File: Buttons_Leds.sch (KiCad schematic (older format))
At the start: 38 parts, among them P11 CONN_01X06, P12 CONN_01X06, Q2 2N7002, Q3 2N7002, Q4 2N7002, Q5 2N7002, SW1 TEC_1, SW2 TEC_1, SW3 TEC_1, SW4 TEC_1

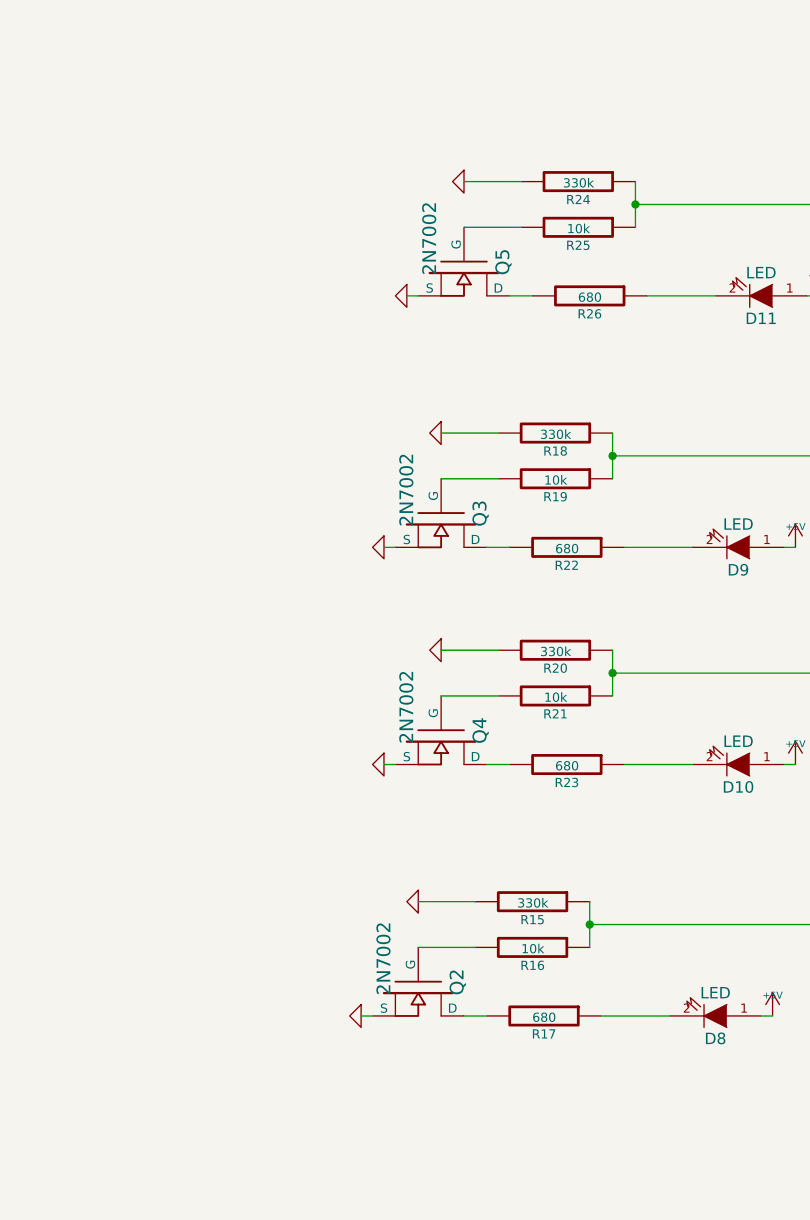
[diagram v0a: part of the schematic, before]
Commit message: Modifico algunos componentes. Seteo algunos encapsulados. Ordeno los componentes en el PCB.
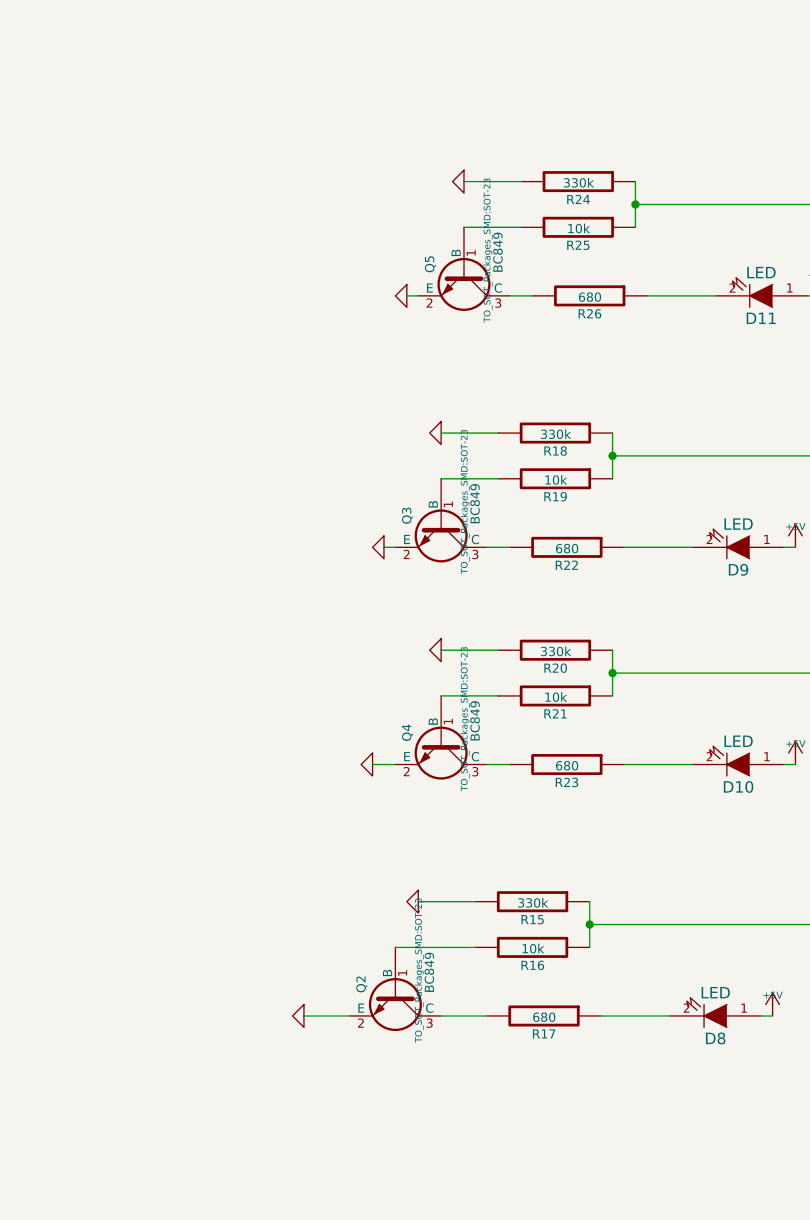
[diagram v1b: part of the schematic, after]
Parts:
- removed Q2, Q3, Q4, Q5: 2N7002, SOT23GDS, symbol MOSFET_N
- added Q2, Q3, Q4, Q5: BC849, TO_SOT_Packages_SMD:SOT-23, symbol BC849
- C10, C11, C12, C9: footprint c_0805 -> Capacitors_SMD:C_0805
- D10, D11, D8, D9: footprint LED-0805 -> LEDs:LED_1206
- P11, P12: footprint (none) -> Pin_Headers:Pin_Header_Angled_1x06
- R10, R11, R12, R13, R14, R15, R16, R17, R18, R19, R20, R21, R22, R23, R24, R25, R26, R7, R8, R9: footprint SM0805 -> SMD_Packages:SMD-1206_Pol
- SW1, SW2, SW3, SW4: footprint PUSH_SWITCH_THT -> Buttons_Switches_SMD:SW_SPST_KMR2
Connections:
- net GND: now also Q2.2 (E), Q3.2 (E), Q4.2 (E), Q5.2 (E)
- net at R23.2: now also Q4.3 (C)
- net at R21.2: now also Q4.1 (B)
- net at R17.2: now also Q2.3 (C)
- net at R16.2: now also Q2.1 (B)
- net at R26.2: now also Q5.3 (C)
- net at R25.2: now also Q5.1 (B)
- net at R22.2: now also Q3.3 (C)
- net at R19.2: now also Q3.1 (B)

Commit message: Algunas modificaciones en el circuito  oreno el pcb.
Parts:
- P11, P12: footprint Pin_Headers:Pin_Header_Angled_1x06 -> Pin_Headers:Pin_Header_Straight_1x06
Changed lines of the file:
@@
 LIBS:video
 LIBS:xilinx
+LIBS:sim800l
 EELAYER 25 0
 EELAYER END
@@
 $EndComp
 $Comp
-L GND #PWR042
+L GND #PWR037
 U 1 1 581A1B02
 P 6050 4250
-F 0 "#PWR042" H 6050 4250 30  0001 C CNN
+F 0 "#PWR037" H 6050 4250 30  0001 C CNN
 F 1 "GND" H 6050 4180 30  0001 C CNN
 F 2 "" H 6050 4250 60  0000 C CNN
@@
 $EndComp
 $Comp
-L +5V #PWR043
+L +5V #PWR038
 U 1 1 581A1B04
 P 7900 4250
-F 0 "#PWR043" H 7900 4340 20  0001 C CNN
+F 0 "#PWR038" H 7900 4340 20  0001 C CNN
 F 1 "+5V" H 7900 4340 30  0000 C CNN
 F 2 "" H 7900 4250 60  0000 C CNN
@@
 $EndComp
 $Comp
-L GND #PWR044
+L GND #PWR039
 U 1 1 581A1B06
 P 6350 3750
-F 0 "#PWR044" H 6350 3750 30  0001 C CNN
+F 0 "#PWR039" H 6350 3750 30  0001 C CNN
 F 1 "GND" H 6350 3680 30  0001 C CNN
 F 2 "" H 6350 3750 60  0000 C CNN
@@
 $EndComp
 $Comp
-L GND #PWR045
+L GND #PWR040
 U 1 1 581A1B0A
 P 1900 7400
-F 0 "#PWR045" H 1900 7400 30  0001 C CNN
+F 0 "#PWR040" H 1900 7400 30  0001 C CNN
 F 1 "GND" H 1900 7330 30  0001 C CNN
 F 2 "" H 1900 7400 60  0000 C CNN
@@
 $EndComp
 $Comp
-L GND #PWR046
+L GND #PWR041
 U 1 1 581A1B0D
 P 2700 7050
-F 0 "#PWR046" H 2700 7050 30  0001 C CNN
+F 0 "#PWR041" H 2700 7050 30  0001 C CNN
 F 1 "GND" H 2700 6980 30  0001 C CNN
 F 2 "" H 2700 7050 60  0000 C CNN
@@
 $EndComp
 $Comp
-L +3,3V #PWR047
+L +3,3V #PWR042
 U 1 1 581A1B0E
 P 1900 6100
-F 0 "#PWR047" H 1900 6060 30  0001 C CNN
+F 0 "#PWR042" H 1900 6060 30  0001 C CNN
 F 1 "+3,3V" H 1900 6210 30  0000 C CNN
 F 2 "" H 1900 6100 60  0000 C CNN
@@
 $EndComp
 $Comp
-L GND #PWR048
+L GND #PWR043
 U 1 1 581A1B11
 P 5750 5350
-F 0 "#PWR048" H 5750 5350 30  0001 C CNN
+F 0 "#PWR043" H 5750 5350 30  0001 C CNN
 F 1 "GND" H 5750 5280 30  0001 C CNN
 F 2 "" H 5750 5350 60  0000 C CNN
@@
 $EndComp
 $Comp
-L +5V #PWR049
+L +5V #PWR044
 U 1 1 581A1B13
 P 7800 5350
-F 0 "#PWR049" H 7800 5440 20  0001 C CNN
+F 0 "#PWR044" H 7800 5440 20  0001 C CNN
 F 1 "+5V" H 7800 5440 30  0000 C CNN
 F 2 "" H 7800 5350 60  0000 C CNN
@@
 $EndComp
 $Comp
-L GND #PWR050
+L GND #PWR045
 U 1 1 581A1B15
 P 6250 4850
-F 0 "#PWR050" H 6250 4850 30  0001 C CNN
+F 0 "#PWR045" H 6250 4850 30  0001 C CNN
 F 1 "GND" H 6250 4780 30  0001 C CNN
 F 2 "" H 6250 4850 60  0000 C CNN
@@
 $EndComp
 $Comp
-L GND #PWR051
+L GND #PWR046
 U 1 1 581A1B19
 P 6200 2200
-F 0 "#PWR051" H 6200 2200 30  0001 C CNN
+F 0 "#PWR046" H 6200 2200 30  0001 C CNN
 F 1 "GND" H 6200 2130 30  0001 C CNN
 F 2 "" H 6200 2200 60  0000 C CNN
@@
 $EndComp
 $Comp
-L +5V #PWR052
+L +5V #PWR047
 U 1 1 581A1B1B
 P 8000 2200
-F 0 "#PWR052" H 8000 2290 20  0001 C CNN
+F 0 "#PWR047" H 8000 2290 20  0001 C CNN
 F 1 "+5V" H 8000 2290 30  0000 C CNN
 F 2 "" H 8000 2200 60  0000 C CNN
@@
 $EndComp
 $Comp
-L GND #PWR053
+L GND #PWR048
 U 1 1 581A1B1D
 P 6450 1700
-F 0 "#PWR053" H 6450 1700 30  0001 C CNN
+F 0 "#PWR048" H 6450 1700 30  0001 C CNN
 F 1 "GND" H 6450 1630 30  0001 C CNN
 F 2 "" H 6450 1700 60  0000 C CNN
@@
 $EndComp
 $Comp
-L GND #PWR054
+L GND #PWR049
 U 1 1 581A1B21
 P 6100 3300
-F 0 "#PWR054" H 6100 3300 30  0001 C CNN
+F 0 "#PWR049" H 6100 3300 30  0001 C CNN
 F 1 "GND" H 6100 3230 30  0001 C CNN
 F 2 "" H 6100 3300 60  0000 C CNN
@@
 $EndComp
 $Comp
-L +5V #PWR055
+L +5V #PWR050
 U 1 1 581A1B23
 P 7900 3300
-F 0 "#PWR055" H 7900 3390 20  0001 C CNN
+F 0 "#PWR050" H 7900 3390 20  0001 C CNN
 F 1 "+5V" H 7900 3390 30  0000 C CNN
 F 2 "" H 7900 3300 60  0000 C CNN
@@
 $EndComp
 $Comp
-L GND #PWR056
+L GND #PWR051
 U 1 1 581A1B25
 P 6350 2800
-F 0 "#PWR056" H 6350 2800 30  0001 C CNN
+F 0 "#PWR051" H 6350 2800 30  0001 C CNN
 F 1 "GND" H 6350 2730 30  0001 C CNN
 F 2 "" H 6350 2800 60  0000 C CNN
@@
 F 0 "P12" H 9250 4000 50  0000 C CNN
 F 1 "CONN_01X06" V 9350 3650 50  0000 C CNN
-F 2 "Pin_Headers:Pin_Header_Angled_1x06" H 9250 3650 50  0001 C CNN
+F 2 "Pin_Headers:Pin_Header_Straight_1x06" H 9250 3650 50  0001 C CNN
 F 3 "" H 9250 3650 50  0000 C CNN
 	1    9250 3650
@@
 $EndComp
 $Comp
-L GND #PWR057
+L GND #PWR052
 U 1 1 581A1B28
 P 8950 4100
-F 0 "#PWR057" H 8950 4100 30  0001 C CNN
+F 0 "#PWR052" H 8950 4100 30  0001 C CNN
 F 1 "GND" H 8950 4030 30  0001 C CNN
 F 2 "" H 8950 4100 60  0000 C CNN
@@
 $EndComp
 $Comp
-L GND #PWR058
+L GND #PWR053
 U 1 1 581A1B29
 P 8950 3250
-F 0 "#PWR058" H 8950 3250 30  0001 C CNN
+F 0 "#PWR053" H 8950 3250 30  0001 C CNN
 F 1 "GND" H 8950 3180 30  0001 C CNN
 F 2 "" H 8950 3250 60  0000 C CNN
@@
 F 0 "P11" H 650 4400 50  0000 C CNN
 F 1 "CONN_01X06" V 750 4050 50  0000 C CNN
-F 2 "Pin_Headers:Pin_Header_Angled_1x06" H 650 4050 50  0001 C CNN
+F 2 "Pin_Headers:Pin_Header_Straight_1x06" H 650 4050 50  0001 C CNN
 F 3 "" H 650 4050 50  0000 C CNN
 	1    650  4050
@@
 Connection ~ 1100 1400
 $Comp
-L GND #PWR059
+L GND #PWR054
 U 1 1 581A1B2B
 P 900 4450
-F 0 "#PWR059" H 900 4450 30  0001 C CNN
+F 0 "#PWR054" H 900 4450 30  0001 C CNN
 F 1 "GND" H 900 4380 30  0001 C CNN
 F 2 "" H 900 4450 60  0000 C CNN
@@
 $EndComp
 $Comp
-L GND #PWR060
+L GND #PWR055
 U 1 1 581A1B2C
 P 950 3700
-F 0 "#PWR060" H 950 3700 30  0001 C CNN
+F 0 "#PWR055" H 950 3700 30  0001 C CNN
 F 1 "GND" H 950 3630 30  0001 C CNN
 F 2 "" H 950 3700 60  0000 C CNN
@@
 $EndComp
 $Comp
-L GND #PWR061
+L GND #PWR056
 U 1 1 581A1B2F
 P 2150 3750
-F 0 "#PWR061" H 2150 3750 30  0001 C CNN
+F 0 "#PWR056" H 2150 3750 30  0001 C CNN
 F 1 "GND" H 2150 3680 30  0001 C CNN
 F 2 "" H 2150 3750 60  0000 C CNN
@@
 $EndComp
 $Comp
-L GND #PWR062
+L GND #PWR057
 U 1 1 581A1B32
 P 2950 3400
-F 0 "#PWR062" H 2950 3400 30  0001 C CNN
+F 0 "#PWR057" H 2950 3400 30  0001 C CNN
 F 1 "GND" H 2950 3330 30  0001 C CNN
 F 2 "" H 2950 3400 60  0000 C CNN
@@
 $EndComp
 $Comp
-L +3,3V #PWR063
+L +3,3V #PWR058
 U 1 1 581A1B33
 P 2150 2450
-F 0 "#PWR063" H 2150 2410 30  0001 C CNN
+F 0 "#PWR058" H 2150 2410 30  0001 C CNN
 F 1 "+3,3V" H 2150 2560 30  0000 C CNN
 F 2 "" H 2150 2450 60  0000 C CNN
@@
 $EndComp
 $Comp
-L GND #PWR064
+L GND #PWR059
 U 1 1 581A1B36
 P 2000 2000
-F 0 "#PWR064" H 2000 2000 30  0001 C CNN
+F 0 "#PWR059" H 2000 2000 30  0001 C CNN
 F 1 "GND" H 2000 1930 30  0001 C CNN
 F 2 "" H 2000 2000 60  0000 C CNN
@@
 $EndComp
 $Comp
-L GND #PWR065
+L GND #PWR060
 U 1 1 581A1B39
 P 2800 1650
-F 0 "#PWR065" H 2800 1650 30  0001 C CNN
+F 0 "#PWR060" H 2800 1650 30  0001 C CNN
 F 1 "GND" H 2800 1580 30  0001 C CNN
 F 2 "" H 2800 1650 60  0000 C CNN
@@
 $EndComp
 $Comp
-L +3,3V #PWR066
+L +3,3V #PWR061
 U 1 1 581A1B3A
 P 2000 700
-F 0 "#PWR066" H 2000 660 30  0001 C CNN
+F 0 "#PWR061" H 2000 660 30  0001 C CNN
 F 1 "+3,3V" H 2000 810 30  0000 C CNN
 F 2 "" H 2000 700 60  0000 C CNN
@@
 $EndComp
 $Comp
-L GND #PWR067
+L GND #PWR062
 U 1 1 581A1B3D
 P 2050 5650
-F 0 "#PWR067" H 2050 5650 30  0001 C CNN
+F 0 "#PWR062" H 2050 5650 30  0001 C CNN
 F 1 "GND" H 2050 5580 30  0001 C CNN
 F 2 "" H 2050 5650 60  0000 C CNN
@@
 $EndComp
 $Comp
-L GND #PWR068
+L GND #PWR063
 U 1 1 581A1B40
 P 2850 5300
-F 0 "#PWR068" H 2850 5300 30  0001 C CNN
+F 0 "#PWR063" H 2850 5300 30  0001 C CNN
 F 1 "GND" H 2850 5230 30  0001 C CNN
 F 2 "" H 2850 5300 60  0000 C CNN
@@
 $EndComp
 $Comp
-L +3,3V #PWR069
+L +3,3V #PWR064
 U 1 1 581A1B41
 P 2050 4350
-F 0 "#PWR069" H 2050 4310 30  0001 C CNN
+F 0 "#PWR064" H 2050 4310 30  0001 C CNN
 F 1 "+3,3V" H 2050 4460 30  0000 C CNN
 F 2 "" H 2050 4350 60  0000 C CNN

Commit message: Modificaciones en el schematic dado los componentes comprados empiezo a ordenar los componentes en una dimension estimada de 10x6 cm.
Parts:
- C10, C11, C12, C9: footprint Capacitors_SMD:C_0805 -> Capacitors_SMD:C_1206
- D10, D11, D8, D9: footprint LEDs:LED_1206 -> Diodes_SMD:MELF_Handsoldering
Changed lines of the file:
@@
 $EndComp
 $Comp
-L GND #PWR038
+L GND #PWR044
 U 1 1 581A1B02
 P 6050 4250
-F 0 "#PWR038" H 6050 4250 30  0001 C CNN
+F 0 "#PWR044" H 6050 4250 30  0001 C CNN
 F 1 "GND" H 6050 4180 30  0001 C CNN
 F 2 "" H 6050 4250 60  0000 C CNN
@@
 $EndComp
 $Comp
-L +5V #PWR039
+L +5V #PWR045
 U 1 1 581A1B04
 P 7900 4250
-F 0 "#PWR039" H 7900 4340 20  0001 C CNN
+F 0 "#PWR045" H 7900 4340 20  0001 C CNN
 F 1 "+5V" H 7900 4340 30  0000 C CNN
 F 2 "" H 7900 4250 60  0000 C CNN
@@
 $EndComp
 $Comp
-L GND #PWR040
+L GND #PWR046
 U 1 1 581A1B06
 P 6350 3750
-F 0 "#PWR040" H 6350 3750 30  0001 C CNN
+F 0 "#PWR046" H 6350 3750 30  0001 C CNN
 F 1 "GND" H 6350 3680 30  0001 C CNN
 F 2 "" H 6350 3750 60  0000 C CNN
@@
 F 0 "D10" H 7650 4350 50  0000 C CNN
 F 1 "LED" H 7650 4150 50  0000 C CNN
-F 2 "LEDs:LED_1206" H 4750 6550 60  0001 C CNN
+F 2 "Diodes_SMD:MELF_Handsoldering" H 4750 6550 60  0001 C CNN
 F 3 "qtlp630c-2.pdf" H 4750 6550 60  0001 C CNN
 F 4 "LED YELLOW WTR CLR 0805 SMD T/R" H 4750 6550 60  0001 C CNN "Descripción"
@@
 $EndComp
 $Comp
-L GND #PWR041
+L GND #PWR047
 U 1 1 581A1B0A
 P 1900 7400
-F 0 "#PWR041" H 1900 7400 30  0001 C CNN
+F 0 "#PWR047" H 1900 7400 30  0001 C CNN
 F 1 "GND" H 1900 7330 30  0001 C CNN
 F 2 "" H 1900 7400 60  0000 C CNN
@@
 F 0 "C9" H 1900 7200 40  0000 L CNN
 F 1 "100nF" H 1906 7015 40  0000 L CNN
-F 2 "Capacitors_SMD:C_0805" H 1238 11100 30  0001 C CNN
+F 2 "Capacitors_SMD:C_1206" H 1238 11100 30  0001 C CNN
 F 3 "KEM_C1002_X7R_SMD.pdf" H 1200 11250 60  0001 C CNN
 F 4 "CAP CER 0.1UF 16V 10% X7R 0805" H 1200 11250 60  0001 C CNN "Descripción"
@@
 $EndComp
 $Comp
-L GND #PWR042
+L GND #PWR048
 U 1 1 581A1B0D
 P 2700 7050
-F 0 "#PWR042" H 2700 7050 30  0001 C CNN
+F 0 "#PWR048" H 2700 7050 30  0001 C CNN
 F 1 "GND" H 2700 6980 30  0001 C CNN
 F 2 "" H 2700 7050 60  0000 C CNN
@@
 $EndComp
 $Comp
-L +3,3V #PWR043
+L +3,3V #PWR049
 U 1 1 581A1B0E
 P 1900 6100
-F 0 "#PWR043" H 1900 6060 30  0001 C CNN
+F 0 "#PWR049" H 1900 6060 30  0001 C CNN
 F 1 "+3,3V" H 1900 6210 30  0000 C CNN
 F 2 "" H 1900 6100 60  0000 C CNN
@@
 $EndComp
 $Comp
-L GND #PWR044
+L GND #PWR050
 U 1 1 581A1B11
 P 5750 5350
-F 0 "#PWR044" H 5750 5350 30  0001 C CNN
+F 0 "#PWR050" H 5750 5350 30  0001 C CNN
 F 1 "GND" H 5750 5280 30  0001 C CNN
 F 2 "" H 5750 5350 60  0000 C CNN
@@
 $EndComp
 $Comp
-L +5V #PWR045
+L +5V #PWR051
 U 1 1 581A1B13
 P 7800 5350
-F 0 "#PWR045" H 7800 5440 20  0001 C CNN
+F 0 "#PWR051" H 7800 5440 20  0001 C CNN
 F 1 "+5V" H 7800 5440 30  0000 C CNN
 F 2 "" H 7800 5350 60  0000 C CNN
@@
 $EndComp
 $Comp
-L GND #PWR046
+L GND #PWR052
 U 1 1 581A1B15
 P 6250 4850
-F 0 "#PWR046" H 6250 4850 30  0001 C CNN
+F 0 "#PWR052" H 6250 4850 30  0001 C CNN
 F 1 "GND" H 6250 4780 30  0001 C CNN
 F 2 "" H 6250 4850 60  0000 C CNN
@@
 F 0 "D8" H 7550 5450 50  0000 C CNN
 F 1 "LED" H 7550 5250 50  0000 C CNN
-F 2 "LEDs:LED_1206" H 4650 7650 60  0001 C CNN
+F 2 "Diodes_SMD:MELF_Handsoldering" H 4650 7650 60  0001 C CNN
 F 3 "qtlp630c-2.pdf" H 4650 7650 60  0001 C CNN
 F 4 "LED YELLOW WTR CLR 0805 SMD T/R" H 4650 7650 60  0001 C CNN "Descripción"
@@
 $EndComp
 $Comp
-L GND #PWR047
+L GND #PWR053
 U 1 1 581A1B19
 P 6200 2200
-F 0 "#PWR047" H 6200 2200 30  0001 C CNN
+F 0 "#PWR053" H 6200 2200 30  0001 C CNN
 F 1 "GND" H 6200 2130 30  0001 C CNN
 F 2 "" H 6200 2200 60  0000 C CNN
@@
 $EndComp
 $Comp
-L +5V #PWR048
+L +5V #PWR054
 U 1 1 581A1B1B
 P 8000 2200
-F 0 "#PWR048" H 8000 2290 20  0001 C CNN
+F 0 "#PWR054" H 8000 2290 20  0001 C CNN
 F 1 "+5V" H 8000 2290 30  0000 C CNN
 F 2 "" H 8000 2200 60  0000 C CNN
@@
 $EndComp
 $Comp
-L GND #PWR049
+L GND #PWR055
 U 1 1 581A1B1D
 P 6450 1700
-F 0 "#PWR049" H 6450 1700 30  0001 C CNN
+F 0 "#PWR055" H 6450 1700 30  0001 C CNN
 F 1 "GND" H 6450 1630 30  0001 C CNN
 F 2 "" H 6450 1700 60  0000 C CNN
@@
 F 0 "D11" H 7750 2300 50  0000 C CNN
 F 1 "LED" H 7750 2100 50  0000 C CNN
-F 2 "LEDs:LED_1206" H 4850 4500 60  0001 C CNN
+F 2 "Diodes_SMD:MELF_Handsoldering" H 4850 4500 60  0001 C CNN
 F 3 "qtlp630c-2.pdf" H 4850 4500 60  0001 C CNN
 F 4 "LED YELLOW WTR CLR 0805 SMD T/R" H 4850 4500 60  0001 C CNN "Descripción"
@@
 $EndComp
 $Comp
-L GND #PWR050
+L GND #PWR056
 U 1 1 581A1B21
 P 6100 3300
-F 0 "#PWR050" H 6100 3300 30  0001 C CNN
+F 0 "#PWR056" H 6100 3300 30  0001 C CNN
 F 1 "GND" H 6100 3230 30  0001 C CNN
 F 2 "" H 6100 3300 60  0000 C CNN
@@
 $EndComp
 $Comp
-L +5V #PWR051
+L +5V #PWR057
 U 1 1 581A1B23
 P 7900 3300
-F 0 "#PWR051" H 7900 3390 20  0001 C CNN
+F 0 "#PWR057" H 7900 3390 20  0001 C CNN
 F 1 "+5V" H 7900 3390 30  0000 C CNN
 F 2 "" H 7900 3300 60  0000 C CNN
@@
 $EndComp
 $Comp
-L GND #PWR052
+L GND #PWR058
 U 1 1 581A1B25
 P 6350 2800
-F 0 "#PWR052" H 6350 2800 30  0001 C CNN
+F 0 "#PWR058" H 6350 2800 30  0001 C CNN
 F 1 "GND" H 6350 2730 30  0001 C CNN
 F 2 "" H 6350 2800 60  0000 C CNN
@@
 F 0 "D9" H 7650 3400 50  0000 C CNN
 F 1 "LED" H 7650 3200 50  0000 C CNN
-F 2 "LEDs:LED_1206" H 4750 5600 60  0001 C CNN
+F 2 "Diodes_SMD:MELF_Handsoldering" H 4750 5600 60  0001 C CNN
 F 3 "qtlp630c-2.pdf" H 4750 5600 60  0001 C CNN
 F 4 "LED YELLOW WTR CLR 0805 SMD T/R" H 4750 5600 60  0001 C CNN "Descripción"
@@
 $EndComp
 $Comp
-L GND #PWR053
+L GND #PWR059
 U 1 1 581A1B28
 P 8950 4100
-F 0 "#PWR053" H 8950 4100 30  0001 C CNN
+F 0 "#PWR059" H 8950 4100 30  0001 C CNN
 F 1 "GND" H 8950 4030 30  0001 C CNN
 F 2 "" H 8950 4100 60  0000 C CNN
@@
 $EndComp
 $Comp
-L GND #PWR054
+L GND #PWR060
 U 1 1 581A1B29
 P 8950 3250
-F 0 "#PWR054" H 8950 3250 30  0001 C CNN
+F 0 "#PWR060" H 8950 3250 30  0001 C CNN
 F 1 "GND" H 8950 3180 30  0001 C CNN
 F 2 "" H 8950 3250 60  0000 C CNN
@@
 Connection ~ 1100 1400
 $Comp
-L GND #PWR055
+L GND #PWR061
 U 1 1 581A1B2B
 P 900 4450
-F 0 "#PWR055" H 900 4450 30  0001 C CNN
+F 0 "#PWR061" H 900 4450 30  0001 C CNN
 F 1 "GND" H 900 4380 30  0001 C CNN
 F 2 "" H 900 4450 60  0000 C CNN
@@
 $EndComp
 $Comp
-L GND #PWR056
+L GND #PWR062
 U 1 1 581A1B2C
 P 950 3700
-F 0 "#PWR056" H 950 3700 30  0001 C CNN
+F 0 "#PWR062" H 950 3700 30  0001 C CNN
 F 1 "GND" H 950 3630 30  0001 C CNN
 F 2 "" H 950 3700 60  0000 C CNN
@@
 $EndComp
 $Comp
-L GND #PWR057
+L GND #PWR063
 U 1 1 581A1B2F
 P 2150 3750
-F 0 "#PWR057" H 2150 3750 30  0001 C CNN
+F 0 "#PWR063" H 2150 3750 30  0001 C CNN
 F 1 "GND" H 2150 3680 30  0001 C CNN
 F 2 "" H 2150 3750 60  0000 C CNN
@@
 F 0 "C12" H 2150 3550 40  0000 L CNN
 F 1 "100nF" H 2156 3365 40  0000 L CNN
-F 2 "Capacitors_SMD:C_0805" H 1488 7450 30  0001 C CNN
+F 2 "Capacitors_SMD:C_1206" H 1488 7450 30  0001 C CNN
 F 3 "KEM_C1002_X7R_SMD.pdf" H 1450 7600 60  0001 C CNN
 F 4 "CAP CER 0.1UF 16V 10% X7R 0805" H 1450 7600 60  0001 C CNN "Descripción"
@@
 $EndComp
 $Comp
-L GND #PWR058
+L GND #PWR064
 U 1 1 581A1B32
 P 2950 3400
-F 0 "#PWR058" H 2950 3400 30  0001 C CNN
+F 0 "#PWR064" H 2950 3400 30  0001 C CNN
 F 1 "GND" H 2950 3330 30  0001 C CNN
 F 2 "" H 2950 3400 60  0000 C CNN
@@
 $EndComp
 $Comp
-L +3,3V #PWR059
+L +3,3V #PWR065
 U 1 1 581A1B33
 P 2150 2450
-F 0 "#PWR059" H 2150 2410 30  0001 C CNN
+F 0 "#PWR065" H 2150 2410 30  0001 C CNN
 F 1 "+3,3V" H 2150 2560 30  0000 C CNN
 F 2 "" H 2150 2450 60  0000 C CNN
@@
 $EndComp
 $Comp
-L GND #PWR060
+L GND #PWR066
 U 1 1 581A1B36
 P 2000 2000
-F 0 "#PWR060" H 2000 2000 30  0001 C CNN
+F 0 "#PWR066" H 2000 2000 30  0001 C CNN
 F 1 "GND" H 2000 1930 30  0001 C CNN
 F 2 "" H 2000 2000 60  0000 C CNN
@@
 F 0 "C10" H 2000 1800 40  0000 L CNN
 F 1 "100nF" H 2006 1615 40  0000 L CNN
-F 2 "Capacitors_SMD:C_0805" H 1338 5700 30  0001 C CNN
+F 2 "Capacitors_SMD:C_1206" H 1338 5700 30  0001 C CNN
 F 3 "KEM_C1002_X7R_SMD.pdf" H 1300 5850 60  0001 C CNN
 F 4 "CAP CER 0.1UF 16V 10% X7R 0805" H 1300 5850 60  0001 C CNN "Descripción"
@@
 $EndComp
 $Comp
-L GND #PWR061
+L GND #PWR067
 U 1 1 581A1B39
 P 2800 1650
-F 0 "#PWR061" H 2800 1650 30  0001 C CNN
+F 0 "#PWR067" H 2800 1650 30  0001 C CNN
 F 1 "GND" H 2800 1580 30  0001 C CNN
 F 2 "" H 2800 1650 60  0000 C CNN
@@
 $EndComp
 $Comp
-L +3,3V #PWR062
+L +3,3V #PWR068
 U 1 1 581A1B3A
 P 2000 700
-F 0 "#PWR062" H 2000 660 30  0001 C CNN
+F 0 "#PWR068" H 2000 660 30  0001 C CNN
 F 1 "+3,3V" H 2000 810 30  0000 C CNN
 F 2 "" H 2000 700 60  0000 C CNN
@@
 $EndComp
 $Comp
-L GND #PWR063
+L GND #PWR069
 U 1 1 581A1B3D
 P 2050 5650
-F 0 "#PWR063" H 2050 5650 30  0001 C CNN
+F 0 "#PWR069" H 2050 5650 30  0001 C CNN
 F 1 "GND" H 2050 5580 30  0001 C CNN
 F 2 "" H 2050 5650 60  0000 C CNN
@@
 F 0 "C11" H 2050 5450 40  0000 L CNN
 F 1 "100nF" H 2056 5265 40  0000 L CNN
-F 2 "Capacitors_SMD:C_0805" H 1388 9350 30  0001 C CNN
+F 2 "Capacitors_SMD:C_1206" H 1388 9350 30  0001 C CNN
 F 3 "KEM_C1002_X7R_SMD.pdf" H 1350 9500 60  0001 C CNN
 F 4 "CAP CER 0.1UF 16V 10% X7R 0805" H 1350 9500 60  0001 C CNN "Descripción"
@@
 $EndComp
 $Comp
-L GND #PWR064
+L GND #PWR070
 U 1 1 581A1B40
 P 2850 5300
-F 0 "#PWR064" H 2850 5300 30  0001 C CNN
+F 0 "#PWR070" H 2850 5300 30  0001 C CNN
 F 1 "GND" H 2850 5230 30  0001 C CNN
 F 2 "" H 2850 5300 60  0000 C CNN
@@
 $EndComp
 $Comp
-L +3,3V #PWR065
+L +3,3V #PWR071
 U 1 1 581A1B41
 P 2050 4350
-F 0 "#PWR065" H 2050 4310 30  0001 C CNN
+F 0 "#PWR071" H 2050 4310 30  0001 C CNN
 F 1 "+3,3V" H 2050 4460 30  0000 C CNN
 F 2 "" H 2050 4350 60  0000 C CNN
